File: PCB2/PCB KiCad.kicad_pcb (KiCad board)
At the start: 2 copper layers, 80.1 x 100.5 mm, 69 parts, among them J1 Conn_01x04, J2 Conn_01x08, J3 Qwiic, J4 Conn_01x04, J5 Conn_01x04, SW1 MCU_RESET, SW2 TRIGGER, U1 OPA2376xxD, U2 NAU7802SGI, U3 AMS1117-3.3, U4 TLC59208FIPWR, U5 ESP32-S3-DEVKITC-1-N8R2

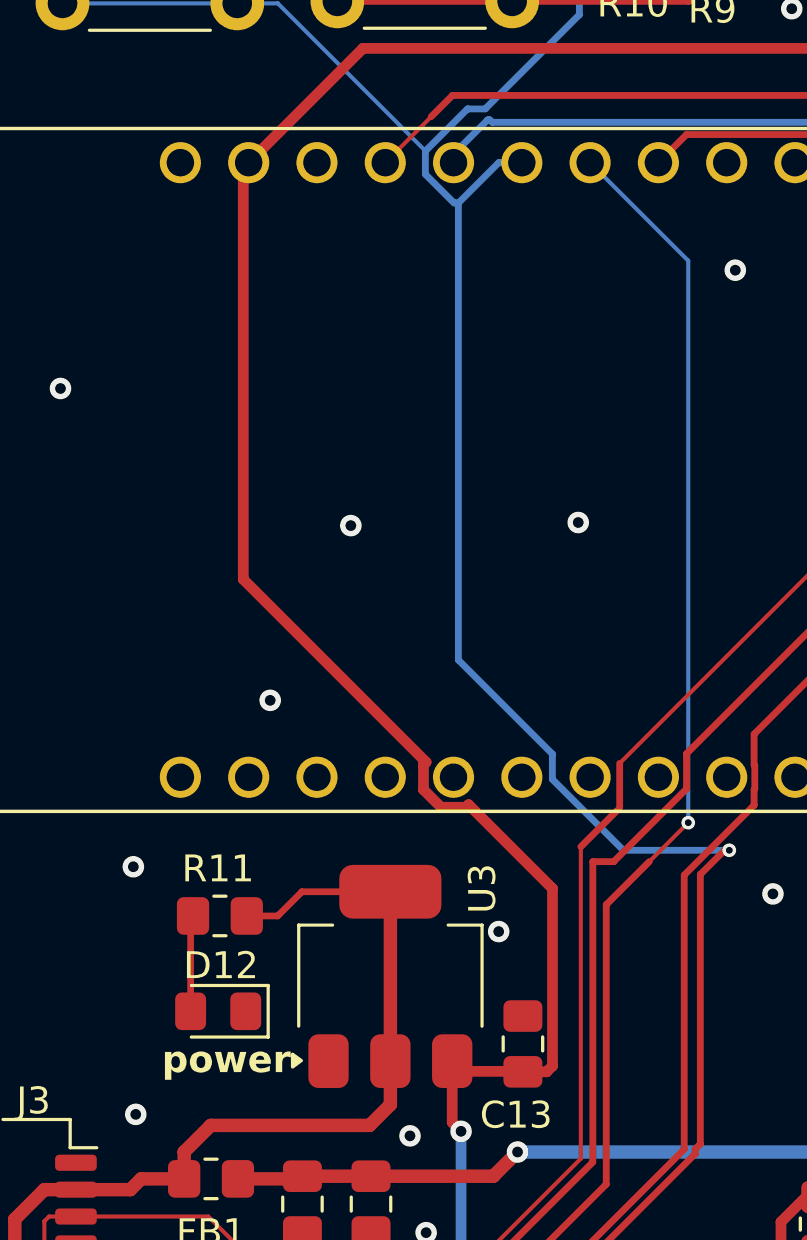
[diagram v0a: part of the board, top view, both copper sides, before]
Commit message: updated pcb traces
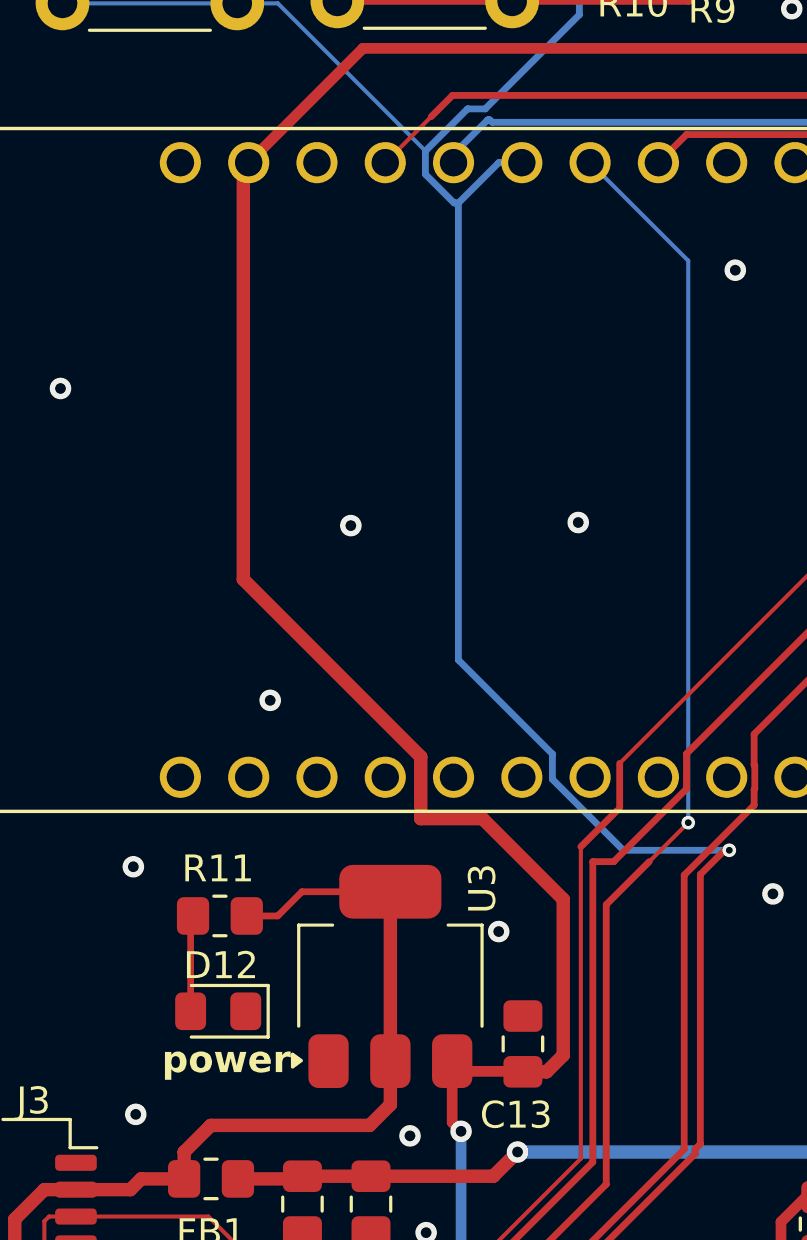
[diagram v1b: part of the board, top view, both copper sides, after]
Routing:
- net +5V: track 141.5 -> 142.3 mm
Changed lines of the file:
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@@
 	)
 	(segment
-		(start 61.2016 95.323257)
-		(end 61.2016 94.396743)
-		(width 0.4)
+		(start 61.1 94.1)
+		(end 54.5 87.5)
+		(width 0.5)
 		(layer "F.Cu")
 		(net 20)
 	)
 	(segment
-		(start 62.880828 95.880828)
-		(end 62.783257 95.9784)
-		(width 0.4)
+		(start 65.7825 105.8175)
+		(end 66.4 105.2)
+		(width 0.5)
+		(layer "F.Cu")
+		(net 20)
+	)
+	(segment
+		(start 63.4 96.4)
+		(end 61.1 96.4)
+		(width 0.5)
 		(layer "F.Cu")
 		(net 20)
@@
 	)
 	(segment
-		(start 62.783257 95.9784)
-		(end 61.856743 95.9784)
+		(start 58.95 67.75)
+		(end 78.115 67.75)
 		(width 0.4)
 		(layer "F.Cu")
@@
 	)
 	(segment
-		(start 58.95 67.75)
-		(end 78.115 67.75)
-		(width 0.4)
+		(start 66.4 99.4)
+		(end 63.4 96.4)
+		(width 0.5)
 		(layer "F.Cu")
 		(net 20)
@@
 	)
 	(segment
-		(start 54.5 87.5)
-		(end 54.5 72.2)
-		(width 0.4)
-		(layer "F.Cu")
-		(net 20)
-	)
-	(segment
 		(start 62.27 107.7)
 		(end 62.6 108.03)
@@
 	)
 	(segment
-		(start 65.7825 105.8175)
-		(end 66 105.6)
-		(width 0.4)
+		(start 64.9 105.8175)
+		(end 65.7825 105.8175)
+		(width 0.5)
+		(layer "F.Cu")
+		(net 20)
+	)
+	(segment
+		(start 61.1 96.4)
+		(end 61.1 94.1)
+		(width 0.5)
+		(layer "F.Cu")
+		(net 20)
+	)
+	(segment
+		(start 54.5 87.5)
+		(end 54.5 72.2)
+		(width 0.5)
 		(layer "F.Cu")
 		(net 20)
@@
 		(start 74.275 62.15)
 		(end 78.115 65.99)
-		(width 0.4)
-		(layer "F.Cu")
-		(net 20)
-	)
-	(segment
-		(start 61.2016 94.396743)
-		(end 61.299171 94.299171)
 		(width 0.4)
 		(layer "F.Cu")
@@
 	)
 	(segment
-		(start 61.299171 94.299171)
-		(end 54.5 87.5)
-		(width 0.4)
-		(layer "F.Cu")
-		(net 20)
-	)
-	(segment
-		(start 61.856743 95.9784)
-		(end 61.2016 95.323257)
-		(width 0.4)
-		(layer "F.Cu")
-		(net 20)
-	)
-	(segment
-		(start 64.9 105.8175)
-		(end 65.7825 105.8175)
-		(width 0.4)
+		(start 66.4 105.2)
+		(end 66.4 99.4)
+		(width 0.5)
 		(layer "F.Cu")
 		(net 20)
@@
 		(start 71.8 62.15)
 		(end 74.625 62.15)
-		(width 0.4)
-		(layer "F.Cu")
-		(net 20)
-	)
-	(segment
-		(start 66 105.6)
-		(end 66 99)
 		(width 0.4)
 		(layer "F.Cu")
@@
 		(width 0.4)
 		(layer "F.Cu")
-		(net 20)
-	)
-	(segment
-		(start 66 99)
-		(end 62.880828 95.880828)
-		(width 0.4)
-		(layer "F.Cu")

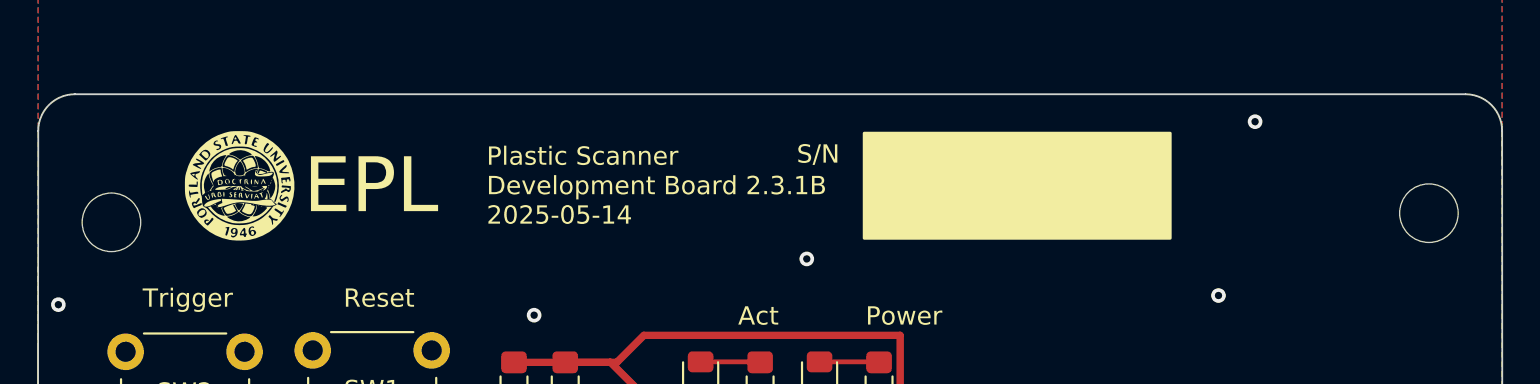
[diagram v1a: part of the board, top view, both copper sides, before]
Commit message: added a github barcode and gerbers files in pcb2 folder
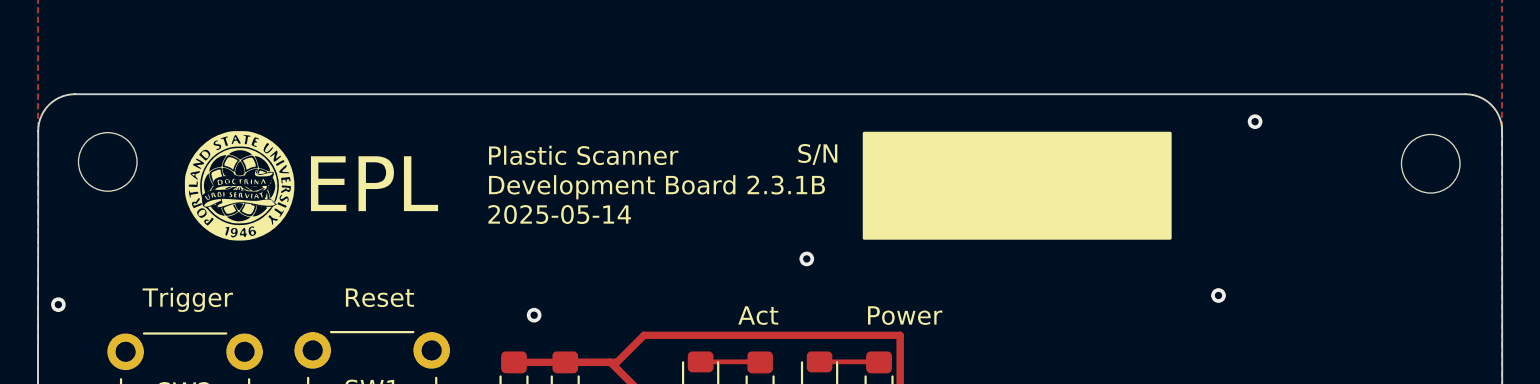
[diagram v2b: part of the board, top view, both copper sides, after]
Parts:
- added G***: LOGO, Github_Barcode:github, B.Cu at (111.7, 61.1)
- moved REF** 3.31 mm to (46.8, 51.2)
- moved ? 2.70 mm to (119.1, 51.3)
